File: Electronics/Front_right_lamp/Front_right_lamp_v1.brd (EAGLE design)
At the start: 42.9 x 26.7 mm, 9 parts

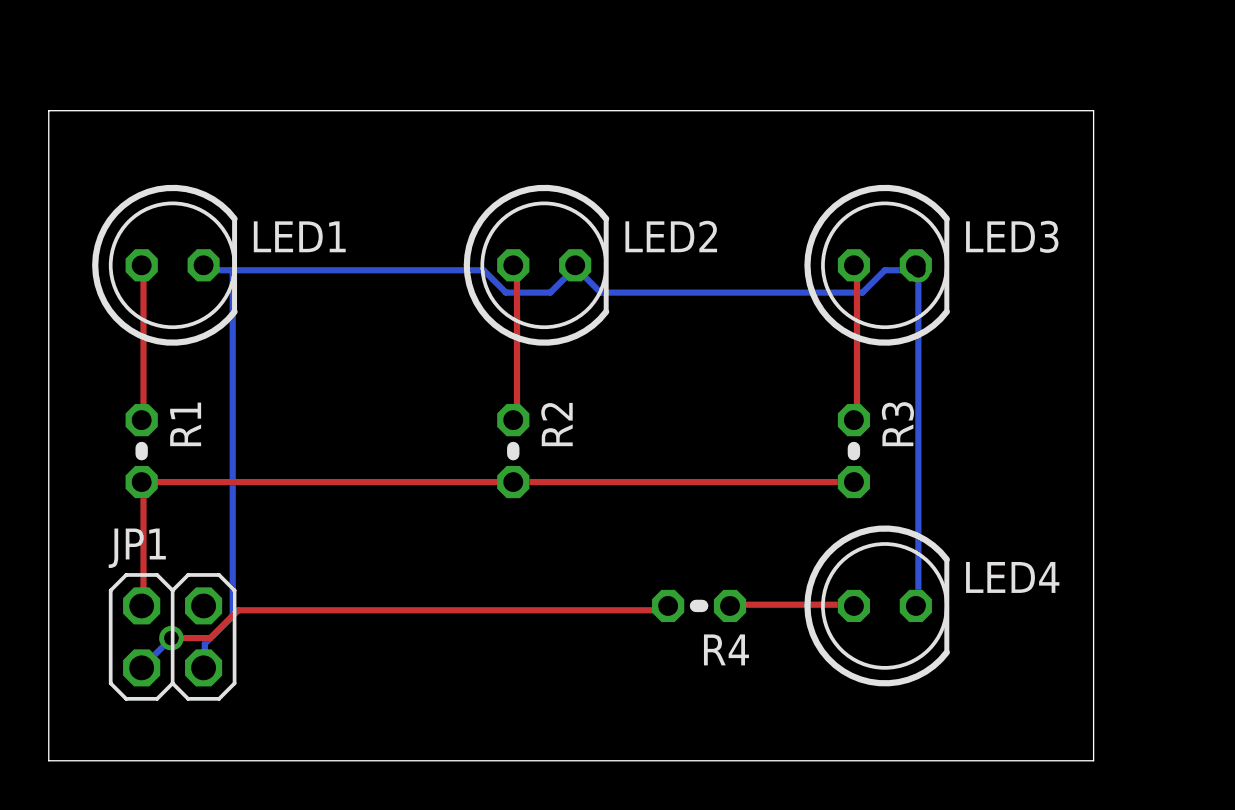
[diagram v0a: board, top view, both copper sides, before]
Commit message: Front lamps done
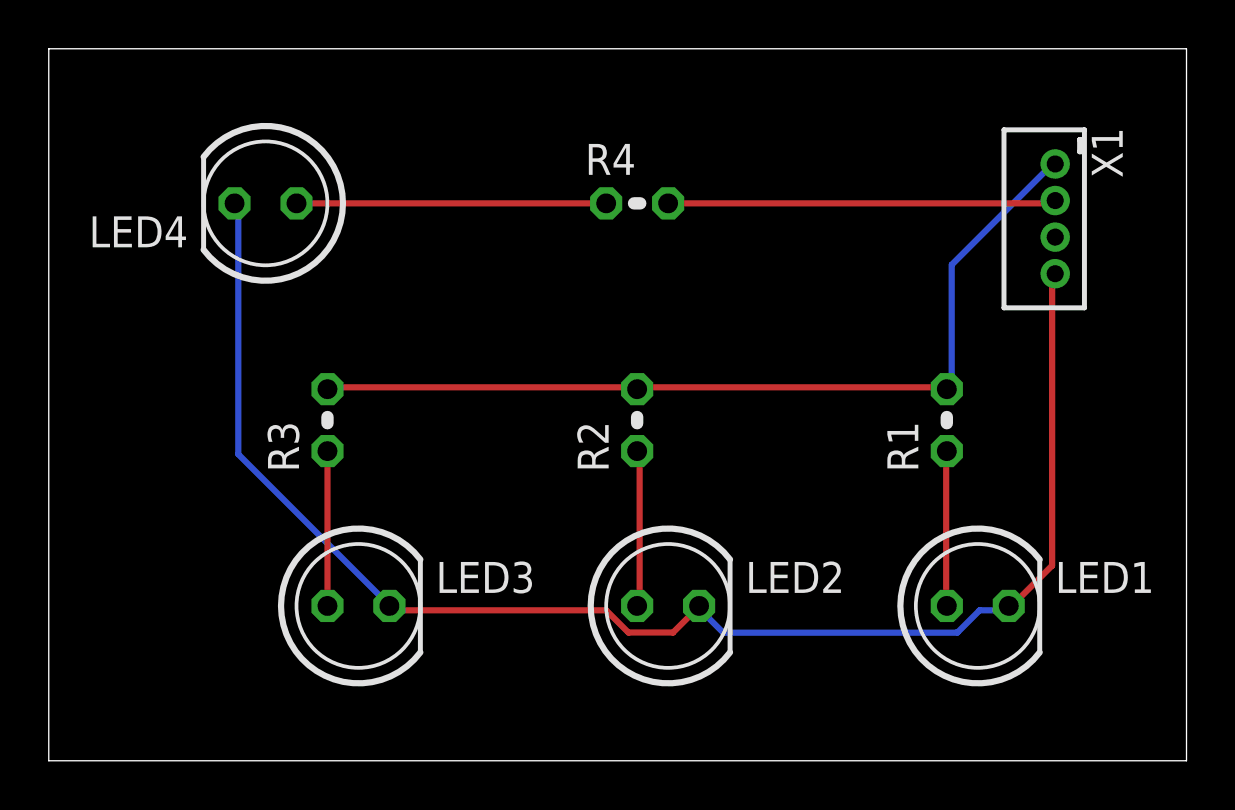
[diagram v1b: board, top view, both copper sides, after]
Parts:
- removed JP1: 2X2, pinhead:2X02
- added X1: B4B-ZR, con-jst:B4B-ZR
- LED1, LED2, LED3: value 2.58V -> 2.58 V
- LED4: value 2.88V -> 1.88 V
- R4: value 1K -> 680
- moved LED1 35.9 mm to (38.1, 6.35)
- moved R1 33.0 mm to (36.8, 14.0), turned to 90 degrees
- moved LED4 30.3 mm to (8.89, 22.9), turned to 180 degrees
- moved LED3 25.7 mm to (12.7, 6.35)
- moved R3 21.6 mm to (11.4, 14.0), turned to 90 degrees
- moved R4 16.7 mm to (24.1, 22.9), turned to 0 degrees
- moved LED2 14.9 mm to (25.4, 6.35)
- moved R2 5.24 mm to (24.1, 14.0), turned to 90 degrees
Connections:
- net N$5: now also X1.1; no longer JP1.2
- net N$6: now also X1.2; no longer JP1.1
- net N$7: now also X1.4; no longer JP1.3
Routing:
- net N$4: track 5.10 -> 12.7 mm
- net N$6: track 22.7 -> 15.9 mm, vias 1 -> 0
- net N$5: track 34.3 -> 36.8 mm
- net N$7: track 62.1 -> 61.0 mm, vias 2 -> 0
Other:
- board size 42.9 x 26.7 mm -> 46.7 x 29.2 mm
